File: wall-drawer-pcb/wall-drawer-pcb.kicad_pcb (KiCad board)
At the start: 2 copper layers, 68.5 x 54 mm, 13 parts, among them J1 Conn_01x04_Pin, J2 Conn_01x04_Pin, J3 Conn_01x02_Pin, J4 Conn_01x02_Pin, J5 Conn_PWRJack_2x5.5mm_CUIDevic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, M1 Module_XIAO-ESP32C3, U1 Regulator_Linear_5.0V_1A_OnSe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

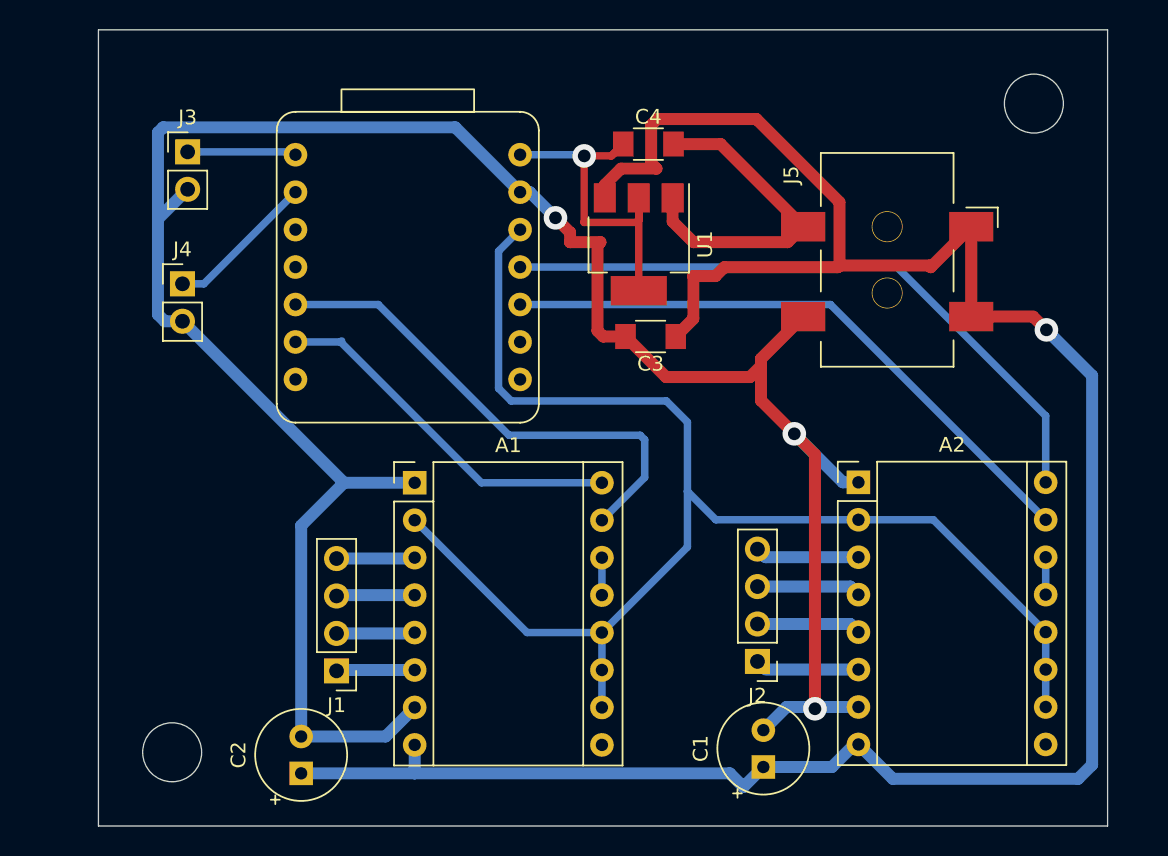
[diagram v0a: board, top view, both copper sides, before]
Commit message: wall drawer pcb to use tmc2209s
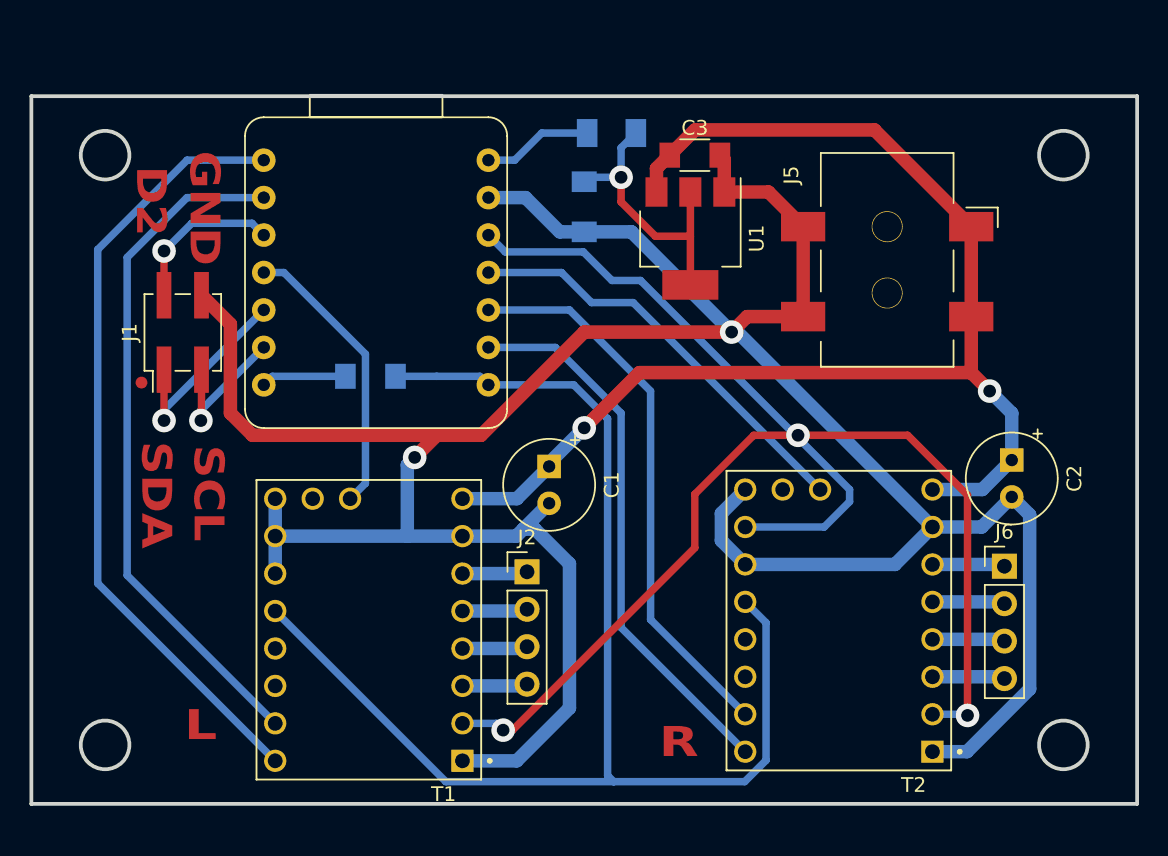
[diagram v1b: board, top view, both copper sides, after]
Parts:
- removed A1, A2: Pololu_Breakout_A4988, Module:Pololu_Breakout-16_15.2x20.3mm
- removed J3, J4: Conn_01x02_Pin, Connector_PinHeader_2.54mm:PinHeader_1x02_P2.54mm_Vertical
- added D1: Diode_Schottky_MiniSMA, fab:Diode_Schottky_MiniSMA, B.Cu at (130.3, 47.0)
- added J6: Conn_01x04_Pin, Connector_PinHeader_2.54mm:PinHeader_1x04_P2.54mm_Vertical, F.Cu at (157.0, 76.4)
- added R1: 1K, fab:R_1206, B.Cu at (114.0, 63.5)
- added T1: ~, TMC2209_SILENTSTEPSTICK:MODULE_TMC2209_SILENTSTEPSTICK, F.Cu at (113.9, 80.7)
- added T2: ~, TMC2209_SILENTSTEPSTICK:MODULE_TMC2209_SILENTSTEPSTICK, F.Cu at (145.8, 80.1)
- C4: moved to B.Cu
- J1: value Conn_01x04_Pin -> Conn_PinHeader_2x02_P2.54mm_Vertical_SMD; footprint Connector_PinHeader_2.54mm:PinHeader_1x04_P2.54mm_Vertical -> fab:PinHeader_2x02_P2.54mm_Vertical_SMD
- moved C2 52.7 mm to (157.5, 69.2), turned to -90 degrees
- moved J1 25.2 mm to (101.3, 60.5), turned to 90 degrees
- moved C1 25.0 mm to (126.1, 69.6), turned to -90 degrees
- moved J2 16.8 mm to (124.6, 76.8), turned to 0 degrees
- moved C3 12.7 mm to (136.0, 48.5), turned to 0 degrees
- moved C4 6.08 mm to (128.5, 52.0), turned to -90 degrees
- moved U1 3.52 mm to (135.7, 54.1)
- moved M1 2.18 mm to (114.4, 56.5)
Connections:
- J1 pad 1: Net-(A1-2B) -> SDA
- J1 pad 2: Net-(A1-2A) -> ANALOG
- J1 pad 3: Net-(A1-1A) -> SCL
- J1 pad 4: Net-(A1-1B) -> GND
- M1 pad 1: D0 -> DIR_L
- M1 pad 10: D9 -> STEP_R
- M1 pad 11: D10 -> DIAG_R
- M1 pad 14: VCC -> Net-(D1-K)
- M1 pad 2: D1 -> STEP_L
- M1 pad 3: unconnected-(M1-D2-Pad3) -> ANALOG
- M1 pad 4: unconnected-(M1-D3-Pad4) -> DIAG_L
- M1 pad 5: D4 -> SDA
- M1 pad 6: D5 -> SCL
- M1 pad 7: unconnected-(M1-D6-Pad7) -> Net-(M1-D6)
- M1 pad 8: unconnected-(M1-D7-Pad8) -> TMC_UART
- M1 pad 9: unconnected-(M1-D8-Pad9) -> DIR_R
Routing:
- net TMC_UART: track 0.00 -> 90.4 mm
- net +12V: track 153.3 -> 88.1 mm, vias 1 -> 2
- net DIR_L: track 0.00 -> 53.4 mm
- net STEP_L: track 0.00 -> 46.7 mm
- net D10: track 44.3 -> 0.00 mm
- net D9: track 41.7 -> 0.00 mm
- net STEP_R: track 0.00 -> 37.9 mm
- net DIR_R: track 0.00 -> 37.3 mm
- net D4: track 34.1 -> 0.00 mm
- net DIAG_R: track 0.00 -> 28.6 mm
- net GND: track 181.5 -> 209.2 mm, vias 3 -> 2
- net D5: track 24.8 -> 0.00 mm
- net DIAG_L: track 0.00 -> 19.4 mm
- net SDA: track 0.00 -> 13.8 mm, vias 0 -> 1
- net ANALOG: track 0.00 -> 10.9 mm, vias 0 -> 1
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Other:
- board size 68.5 x 54 mm -> 75 x 48 mm
- board text added: "D2"
- board text added: "GND"
- board text added: "L"
- board text added: "R"
- board text added: "SCL"
- board text added: "SDA"
